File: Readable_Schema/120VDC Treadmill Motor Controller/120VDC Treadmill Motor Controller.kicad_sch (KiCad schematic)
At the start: 0 parts

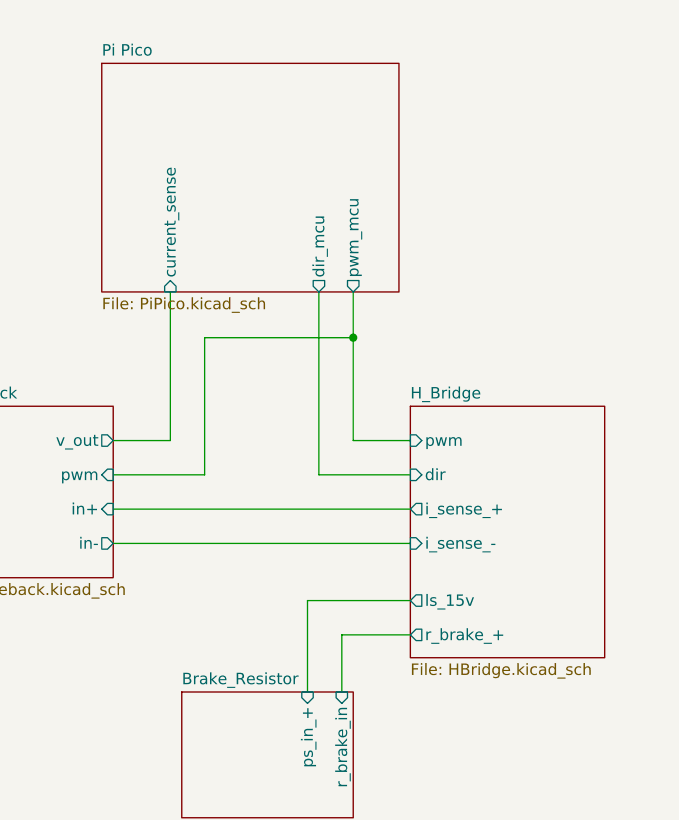
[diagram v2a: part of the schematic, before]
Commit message: Changed ground naming and redid a bit of the pinouts between the pico and the h bridge -- need to fix the feedback loop to use a or gate for pwm_a and pwm_b to combine to one big reset
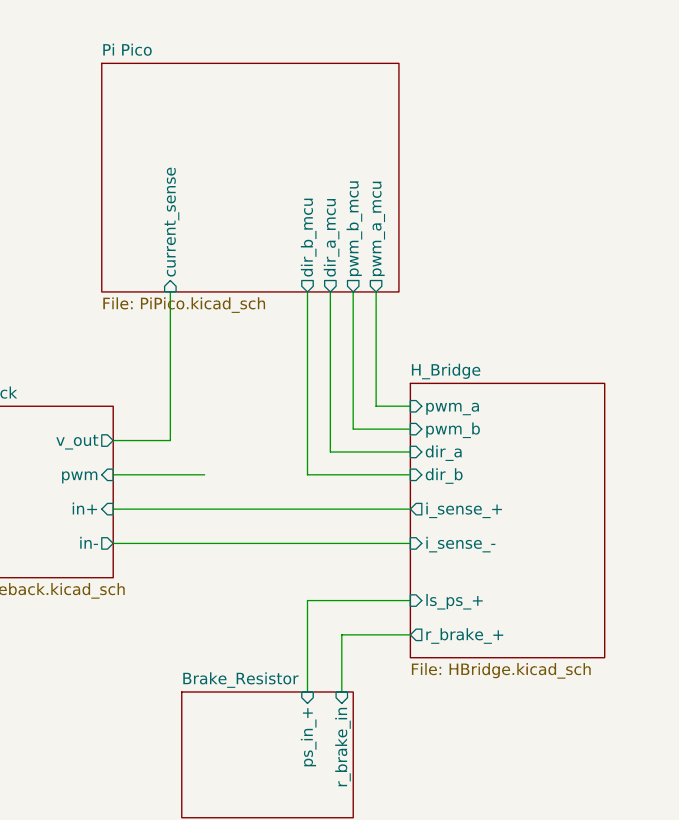
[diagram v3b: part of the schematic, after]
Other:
- sheet H_Bridge ports: added dir_a, dir_b, ls_ps_+, pwm_a, pwm_b; removed dir, ls_15v, pwm
- sheet Pi Pico ports: added dir_a_mcu, dir_b_mcu, pwm_a_mcu, pwm_b_mcu; removed dir_mcu, pwm_mcu
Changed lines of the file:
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@@
 	(generator_version "9.0")
 	(paper "A4")
-	(junction
-		(at 149.86 88.9)
-		(diameter 0)
-		(color 0 0 0 0)
-	)
-	(wire
-		(pts
-			(xy 133.35 104.14) (xy 133.35 88.9)
-		)
-		(stroke
-			(width 0)
-			(type default)
-		)
-	)
 	(wire
 		(pts
@@
 	(wire
 		(pts
+			(xy 144.78 104.14) (xy 156.21 104.14)
+		)
+		(stroke
+			(width 0)
+			(type default)
+		)
+	)
+	(wire
+		(pts
 			(xy 123.19 104.14) (xy 133.35 104.14)
 		)
@@
 	(wire
 		(pts
-			(xy 146.05 83.82) (xy 146.05 104.14)
-		)
-		(stroke
-			(width 0)
-			(type default)
-		)
-	)
-	(wire
-		(pts
 			(xy 148.59 121.92) (xy 156.21 121.92)
 		)
@@
 	(wire
 		(pts
-			(xy 149.86 88.9) (xy 149.86 83.82)
-		)
-		(stroke
-			(width 0)
-			(type default)
-		)
-	)
-	(wire
-		(pts
-			(xy 156.21 100.33) (xy 149.86 100.33)
+			(xy 152.4 83.82) (xy 152.4 96.52)
+		)
+		(stroke
+			(width 0)
+			(type default)
+		)
+	)
+	(wire
+		(pts
+			(xy 152.4 96.52) (xy 156.21 96.52)
+		)
+		(stroke
+			(width 0)
+			(type default)
+		)
+	)
+	(wire
+		(pts
+			(xy 147.32 101.6) (xy 156.21 101.6)
+		)
+		(stroke
+			(width 0)
+			(type default)
+		)
+	)
+	(wire
+		(pts
+			(xy 149.86 83.82) (xy 149.86 99.06)
+		)
+		(stroke
+			(width 0)
+			(type default)
+		)
+	)
+	(wire
+		(pts
+			(xy 144.78 83.82) (xy 144.78 104.14)
+		)
+		(stroke
+			(width 0)
+			(type default)
+		)
+	)
+	(wire
+		(pts
+			(xy 149.86 99.06) (xy 156.21 99.06)
+		)
+		(stroke
+			(width 0)
+			(type default)
+		)
+	)
+	(wire
+		(pts
+			(xy 147.32 83.82) (xy 147.32 101.6)
 		)
 		(stroke
@@
 	(wire
 		(pts
-			(xy 149.86 88.9) (xy 149.86 100.33)
-		)
-		(stroke
-			(width 0)
-			(type default)
-		)
-	)
-	(wire
-		(pts
 			(xy 144.78 118.11) (xy 156.21 118.11)
 		)
@@
 		(pts
 			(xy 148.59 128.27) (xy 148.59 121.92)
-		)
-		(stroke
-			(width 0)
-			(type default)
-		)
-	)
-	(wire
-		(pts
-			(xy 133.35 88.9) (xy 149.86 88.9)
-		)
-		(stroke
-			(width 0)
-			(type default)
-		)
-	)
-	(wire
-		(pts
-			(xy 146.05 104.14) (xy 156.21 104.14)
 		)
 		(stroke
@@
 	)
 	(sheet
-		(at 156.21 96.52)
-		(size 21.59 27.94)
+		(at 156.21 93.98)
+		(size 21.59 30.48)
 		(exclude_from_sim no)
 		(in_bom yes)
@@
 		)
 		(property "Sheetname" "H_Bridge"
-			(at 156.21 95.8084 0)
+			(at 156.21 93.2684 0)
 			(effects
 				(font
@@
 			)
 		)
-		(pin "dir" input
-			(at 156.21 104.14 180)
-			(effects
-				(font
-					(size 1.27 1.27)
-				)
-				(justify left)
-			)
-		)
 		(pin "i_sense_+" output
 			(at 156.21 107.95 180)
@@
 			)
 		)
-		(pin "ls_15v" output
-			(at 156.21 118.11 180)
-			(effects
-				(font
-					(size 1.27 1.27)
-				)
-				(justify left)
-			)
-		)
-		(pin "pwm" input
-			(at 156.21 100.33 180)
-			(effects
-				(font
-					(size 1.27 1.27)
-				)
-				(justify left)
-			)
-		)
 		(pin "r_brake_+" output
 			(at 156.21 121.92 180)
+			(effects
+				(font
+					(size 1.27 1.27)
+				)
+				(justify left)
+			)
+		)
+		(pin "dir_a" input
+			(at 156.21 101.6 180)
+			(effects
+				(font
+					(size 1.27 1.27)
+				)
+				(justify left)
+			)
+		)
+		(pin "dir_b" input
+			(at 156.21 104.14 180)
+			(effects
+				(font
+					(size 1.27 1.27)
+				)
+				(justify left)
+			)
+		)
+		(pin "ls_ps_+" input
+			(at 156.21 118.11 180)
+			(effects
+				(font
+					(size 1.27 1.27)
+				)
+				(justify left)
+			)
+		)
+		(pin "pwm_a" input
+			(at 156.21 96.52 180)
+			(effects
+				(font
+					(size 1.27 1.27)
+				)
+				(justify left)
+			)
+		)
+		(pin "pwm_b" input
+			(at 156.21 99.06 180)
 			(effects
 				(font
@@
 			)
 		)
-		(pin "pwm_mcu" output
+		(pin "dir_a_mcu" output
+			(at 147.32 83.82 270)
+			(effects
+				(font
+					(size 1.27 1.27)
+				)
+				(justify left)
+			)
+		)
+		(pin "dir_b_mcu" output
+			(at 144.78 83.82 270)
+			(effects
+				(font
+					(size 1.27 1.27)
+				)
+				(justify left)
+			)
+		)
+		(pin "pwm_a_mcu" output
+			(at 152.4 83.82 270)
+			(effects
+				(font
+					(size 1.27 1.27)
+				)
+				(justify left)
+			)
+		)
+		(pin "pwm_b_mcu" output
 			(at 149.86 83.82 270)
 			(effects
 				(font
-					(size 1.27 1.27)
-				)
-				(justify left)
-			)
-		)
-		(pin "dir_mcu" output
-			(at 146.05 83.82 270)
-			(effects
-				(font
